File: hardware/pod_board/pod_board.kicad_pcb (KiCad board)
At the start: 4 copper layers, 80 x 55 mm, 0 parts

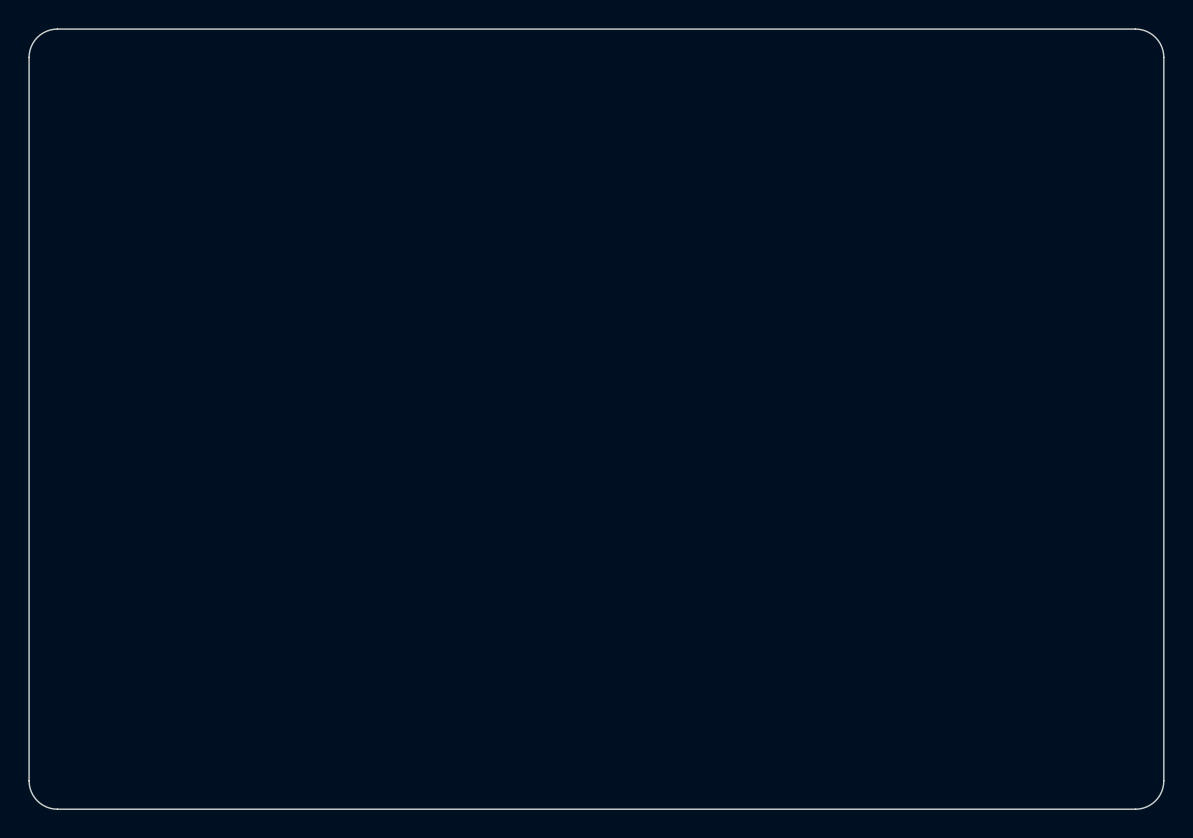
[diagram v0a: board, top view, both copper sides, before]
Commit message: PCBs routed, labelled and ready to order: Rev 1 fabrication files and buy list
Both boards placed, routed and finished by script (hardware/gen): layout.sh places
(placement.py, with silkscreen names for every terminal, port, header and button),
route.sh routes with Freerouting inside rule areas and net classes from the layout
guide and keeps a board only with 0 DRC errors, 0 unconnected and exact schematic
parity, routespec.sh checks what the DRC cannot (planes, crystal, converter loop,
IPC-2221 widths), finish.sh adds the bottom-silkscreen identification and writes
the fabrication files (gerbers, drill, BOM, positions) only when the DRC passes.

- Pod 70 x 53 mm, 4 layers: In1 solid GND, In2 +3V3, 530 teardrops; no DRC warnings.
- Power 95 x 66 mm, 2 layers, 2 oz: 10 A rail as a zone, converter re-placed (switch
  node 16 mm, feedback 7 mm, no vias; was 78 mm and 40 mm), 328 teardrops.
- Screw terminals turned to open outward; RESET/BOOT side-push on the pod's left
  edge; USB-C footprint with a 3D model (GCT USB4105).
- Pod J2 now the Adafruit 4754's JP1 row pin for pin (the old order shorted its
  3.3 V output to ground); IMU reset on a new J8; HC-05 header fed 5 V.
- Buy list per footprint and module connections in bill-of-materials.md section 10.
- LAYOUT_GUIDE rewritten as how the boards were routed and how to review them;
  decisions, progress log and BUILD_GUIDE updated; power box follows the wider board.
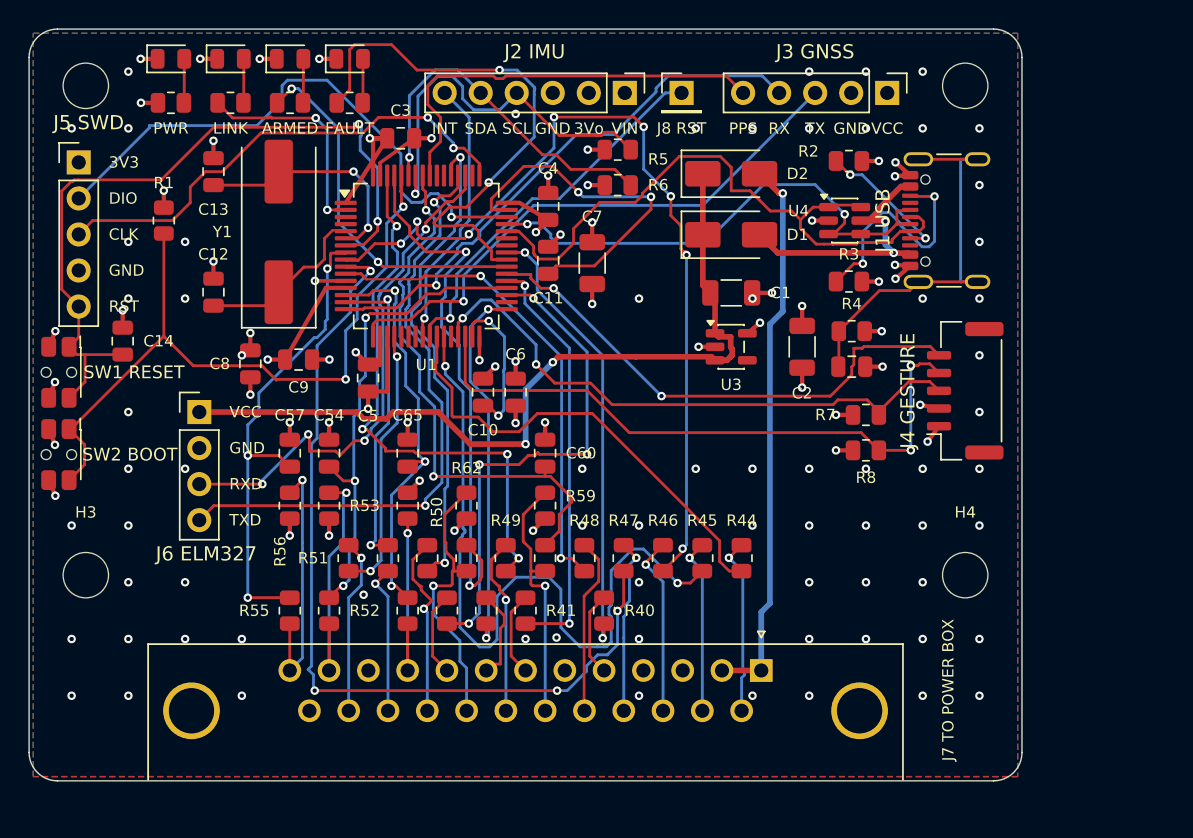
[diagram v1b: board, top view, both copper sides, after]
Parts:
- added C1: 10u, Capacitor_SMD:C_1206_3216Metric, F.Cu at (99.5, 68.6)
- added C10: 2.2u, Capacitor_SMD:C_0805_2012Metric, F.Cu at (82.0, 75.6)
- added C11: 2.2u, Capacitor_SMD:C_0805_2012Metric, F.Cu at (86.6, 66.3)
- added C12: 15p, Capacitor_SMD:C_0805_2012Metric, F.Cu at (63.0, 68.5)
- added C13: 15p, Capacitor_SMD:C_0805_2012Metric, F.Cu at (63.0, 60.0)
- added C14: 100n, Capacitor_SMD:C_0805_2012Metric, F.Cu at (56.6, 72.0)
- added C15: 4.7n, Capacitor_SMD:C_0805_2012Metric, F.Cu at (108.0, 73.8)
- added C2: 10u, Capacitor_SMD:C_1206_3216Metric, F.Cu at (104.5, 72.4)
- added C3: 100n, Capacitor_SMD:C_0805_2012Metric, F.Cu at (76.2, 57.7)
- added C4: 100n, Capacitor_SMD:C_0805_2012Metric, F.Cu at (86.6, 62.5)
- added C5: 100n, Capacitor_SMD:C_0805_2012Metric, F.Cu at (73.9, 74.6)
- added C54: 10n, Capacitor_SMD:C_0805_2012Metric, F.Cu at (71.2, 79.9)
- added C57: 10n, Capacitor_SMD:C_0805_2012Metric, F.Cu at (68.4, 79.9)
- added C6: 100n, Capacitor_SMD:C_0805_2012Metric, F.Cu at (84.3, 75.6)
- added C60: 10n, Capacitor_SMD:C_0805_2012Metric, F.Cu at (86.4, 79.9)
- added C65: 100n, Capacitor_SMD:C_0805_2012Metric, F.Cu at (76.7, 79.9)
- added C7: 4.7u, Capacitor_SMD:C_1206_3216Metric, F.Cu at (89.7, 66.5)
- added C8: 1u, Capacitor_SMD:C_0805_2012Metric, F.Cu at (65.6, 73.6)
- added C9: 100n, Capacitor_SMD:C_0805_2012Metric, F.Cu at (69.0, 73.3)
- added D1: SS14, Diode_SMD:D_SMA, F.Cu at (99.5, 64.5)
- added D2: SS14, Diode_SMD:D_SMA, F.Cu at (99.5, 60.2)
- added D3: green, LED_SMD:LED_0805_2012Metric, F.Cu at (60.0, 52.1)
- added D4: blue, LED_SMD:LED_0805_2012Metric, F.Cu at (64.2, 52.1)
- added D5: amber, LED_SMD:LED_0805_2012Metric, F.Cu at (68.4, 52.1)
- added D6: red, LED_SMD:LED_0805_2012Metric, F.Cu at (72.6, 52.1)
- added H1: M3, MountingHole:MountingHole_3.2mm_M3, F.Cu at (54.0, 54.0)
- added H2: M3, MountingHole:MountingHole_3.2mm_M3, F.Cu at (116.0, 54.0)
- added H3: M3, MountingHole:MountingHole_3.2mm_M3, F.Cu at (54.0, 88.5)
- added H4: M3, MountingHole:MountingHole_3.2mm_M3, F.Cu at (116.0, 88.5)
- added J1: USB-C, Connector_USB:USB_C_Receptacle_GCT_USB4105-xx-A_16P_TopMnt_Horizontal, F.Cu at (115.8, 63.5)
- added J2: IMU (BNO085 breakout), Connector_PinHeader_2.54mm:PinHeader_1x06_P2.54mm_Vertical, F.Cu at (92.0, 54.5)
- added J3: GNSS (NEO-M8N breakout), Connector_PinHeader_2.54mm:PinHeader_1x05_P2.54mm_Vertical, F.Cu at (110.5, 54.5)
- added J4: Gesture puck (JST-GH), Connector_JST:JST_GH_SM05B-GHS-TB_1x05-1MP_P1.25mm_Horizontal, F.Cu at (116.0, 75.5)
- added J5: SWD (ST-Link), Connector_PinHeader_2.54mm:PinHeader_1x05_P2.54mm_Vertical, F.Cu at (53.5, 59.4)
- added J6: ELM327 fallback (USART3), Connector_PinHeader_2.54mm:PinHeader_1x04_P2.54mm_Vertical, F.Cu at (62.0, 77.0)
- added J7: DB-25 to power box, Connector_Dsub:DSUB-25_Socket_Horizontal_P2.77x2.84mm_EdgePinOffset4.94mm_Housed_MountingHolesOffset4.94mm, F.Cu at (101.6, 95.2)
- added J8: IMU reset (optional wire), Connector_PinHeader_2.54mm:PinHeader_1x01_P2.54mm_Vertical, F.Cu at (96.0, 54.5)
- added R1: 10k, Resistor_SMD:R_0805_2012Metric, F.Cu at (59.5, 63.5)
- added R2: 5.1k, Resistor_SMD:R_0805_2012Metric, F.Cu at (107.8, 59.3)
- added R3: 5.1k, Resistor_SMD:R_0805_2012Metric, F.Cu at (107.8, 67.8)
- added R30: 1k, Resistor_SMD:R_0805_2012Metric, F.Cu at (60.0, 55.2)
- added R31: 1k, Resistor_SMD:R_0805_2012Metric, F.Cu at (64.2, 55.2)
- added R32: 1k, Resistor_SMD:R_0805_2012Metric, F.Cu at (68.4, 55.2)
- added R33: 1k, Resistor_SMD:R_0805_2012Metric, F.Cu at (72.6, 55.2)
- added R4: 1M, Resistor_SMD:R_0805_2012Metric, F.Cu at (108.0, 71.3)
- added R40: 1k, Resistor_SMD:R_0805_2012Metric, F.Cu at (90.5, 91.0)
- added R41: 1k, Resistor_SMD:R_0805_2012Metric, F.Cu at (85.0, 91.0)
- added R42: 1k, Resistor_SMD:R_0805_2012Metric, F.Cu at (82.2, 91.0)
- added R43: 1k, Resistor_SMD:R_0805_2012Metric, F.Cu at (79.5, 91.0)
- added R44: 1k, Resistor_SMD:R_0805_2012Metric, F.Cu at (100.2, 87.3)
- added R45: 1k, Resistor_SMD:R_0805_2012Metric, F.Cu at (97.5, 87.3)
- added R46: 1k, Resistor_SMD:R_0805_2012Metric, F.Cu at (94.7, 87.3)
- added R47: 1k, Resistor_SMD:R_0805_2012Metric, F.Cu at (91.9, 87.3)
- added R48: 1k, Resistor_SMD:R_0805_2012Metric, F.Cu at (89.2, 87.3)
- added R49: 330, Resistor_SMD:R_0805_2012Metric, F.Cu at (83.6, 87.3)
- added R5: 4.7k, Resistor_SMD:R_0805_2012Metric, F.Cu at (91.5, 58.5)
- added R50: 1k, Resistor_SMD:R_0805_2012Metric, F.Cu at (78.1, 87.3)
- added R51: 1k, Resistor_SMD:R_0805_2012Metric, F.Cu at (72.5, 87.3)
- added R52: 1k, Resistor_SMD:R_0805_2012Metric, F.Cu at (71.2, 91.0)
- added R53: 10k, Resistor_SMD:R_0805_2012Metric, F.Cu at (71.2, 83.6)
- added R55: 1k, Resistor_SMD:R_0805_2012Metric, F.Cu at (68.4, 91.0)
- added R56: 10k, Resistor_SMD:R_0805_2012Metric, F.Cu at (68.4, 83.6)
- added R58: 1k, Resistor_SMD:R_0805_2012Metric, F.Cu at (86.4, 87.3)
- added R59: 10k, Resistor_SMD:R_0805_2012Metric, F.Cu at (86.4, 83.6)
- added R6: 4.7k, Resistor_SMD:R_0805_2012Metric, F.Cu at (91.5, 61.0)
- added R61: 100, Resistor_SMD:R_0805_2012Metric, F.Cu at (80.8, 87.3)
- added R62: 10k, Resistor_SMD:R_0805_2012Metric, F.Cu at (80.8, 83.6)
- added R63: 100, Resistor_SMD:R_0805_2012Metric, F.Cu at (75.3, 87.3)
- added R64: 1k, Resistor_SMD:R_0805_2012Metric, F.Cu at (76.7, 91.0)
- added R66: 100k, Resistor_SMD:R_0805_2012Metric, F.Cu at (76.7, 83.6)
- added R7: 2.2k, Resistor_SMD:R_0805_2012Metric, F.Cu at (109.0, 77.2)
- added R8: 2.2k, Resistor_SMD:R_0805_2012Metric, F.Cu at (109.0, 79.7)
- added SW1: RESET, Button_Switch_SMD:SW_SPST_EVQP7C, F.Cu at (52.1, 74.2)
- added SW2: BOOT, Button_Switch_SMD:SW_SPST_EVQP7C, F.Cu at (52.1, 80.0)
- added U1: STM32F405RGT6, Package_QFP:LQFP-64_10x10mm_P0.5mm, F.Cu at (78.0, 66.0)
- added U3: AP2112K-3.3, Package_TO_SOT_SMD:SOT-23-5, F.Cu at (99.5, 72.4)
- added U4: USBLC6-2SC6, Package_TO_SOT_SMD:SOT-23-6, F.Cu at (107.5, 63.5)
- added Y1: 8MHz, Crystal:Crystal_SMD_HC49-SD, F.Cu at (67.6, 64.3)
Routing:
- net /RELAY_HAZARD: track 0.00 -> 61.9 mm, vias 0 -> 8
- net /RELAY_HORN: track 0.00 -> 61.9 mm, vias 0 -> 4
- net /VIN_POD: track 0.00 -> 58.1 mm, vias 0 -> 2
- net GND: track 0.00 -> 54.4 mm, vias 0 -> 109
- net /RELAY_RIGHT: track 0.00 -> 53.6 mm, vias 0 -> 2
- net /NRST: track 0.00 -> 53.0 mm, vias 0 -> 2
- net +3V3: track 0.00 -> 52.3 mm, vias 0 -> 22
- net /MCU: STM32F405RGT6/BOOT0: track 0.00 -> 51.4 mm, vias 0 -> 2
- net /GEST_SDA: track 0.00 -> 44.9 mm, vias 0 -> 2
- net /USB_DM: track 0.00 -> 44.9 mm
- net /OBD_RX: track 0.00 -> 43.5 mm, vias 0 -> 2
- net /GEST_SCL: track 0.00 -> 41.3 mm, vias 0 -> 2
- net /SWDIO: track 0.00 -> 40.8 mm, vias 0 -> 1
- net /GPS_RX: track 0.00 -> 39.9 mm, vias 0 -> 1
- net /CAN_TX: track 0.00 -> 39.7 mm, vias 0 -> 4
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- added copper zone on In2.Cu, net +3V3
- added copper zone on B.Cu, net GND
- added copper zone on F.Cu, net GND
- added copper zone on In1.Cu, net GND
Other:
- board size 80 x 55 mm -> 70 x 53 mm
- board text added: "3V3"
- board text added: "3Vo"
- board text added: "AR WINDSCREEN - POD BOARD"
- board text added: "ARMED"
- board text added: "CLK"
- board text added: "DIO"
- board text added: "FAULT"
- board text added: "GND"
- board text added: "Gesture cable (J4): right edge, below the USB"
- board text added: "I. K. MWENDA (FINAL YEAR PROJECT)"
- board text added: "INT"
- board text added: "J1 USB"
- board text added: "J2 IMU"
- board text added: "J3 GNSS"
- board text added: "J4 GESTURE"
- board text added: "J5 SWD"
- board text added: "J6 ELM327"
- board text added: "J7 TO POWER BOX"
- board text added: "J8 RST"
- board text added: "LINK"
- board text added: "PPS"
- board text added: "PWR"
- board text added: "REV 1 2026-10"
- board text added: "RST"
- board text added: "RX"
- board text added: "RXD"
- board text added: "SCL"
- board text added: "SDA"
- board text added: "SW1 RESET"
- board text added: "SW2 BOOT"
- board text added: "SWD header (J5) and the RESET/BOOT plungers (SW1, SW2): left edge"
- board text added: "TX"
- board text added: "TXD"
- board text added: "VCC"
- board text added: "VIN"
- board text added: "pod_board: 70 x 53 mm, 4 layers. 4 layers: signal / GND / +3V3 / signal. Ground plane unbroken under GNSS and IMU. Outline and holes from hardware/gen/outlines.py (shared with the enclosures)."
- board text removed: "SWD (J5) and ELM327 (J6) headers: left edge"
- board text removed: "pod_board: 80 x 55 mm, 4 layers. 4 layers: signal / GND / +3V3 / signal. Ground plane unbroken under GNSS and IMU. Outline and holes from hardware/gen/outlines.py (shared with the enclosures)."

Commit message: Review fixes: no via in SMD pads, 0.6 mm round terminal pins; 5 V converter simulated
An engineer's review of the Rev 1 boards: a via on a ground pad, and thin tracks
close to the screw terminals. Both measured true (9 vias touching ground pads on
the power board, 2 on the pod; 5 places within 0.3 mm of a terminal pin).

- route.py: no via touches any surface-mount pad (stitching and mending had let a
  via sit on its own net's pad); 0.6 mm round terminal and fuse-holder pins, given
  to Freerouting as grown pad copies (KiCad does not export a pad's own clearance);
  layout.py sets that clearance on the real pads for the DRC.
- routespec.sh checks both rules; both boards rerouted, teardrops re-added,
  finished: DRC 0 errors, 0 unconnected, parity exact; all checks pass.
- hardware/sim: the power board's TPS54360 converter simulated with TI's own
  transient model and the board's values, in KiCad's ngspice (no install):
  start-up, a 0.2-1.5 A load step (stability) and 9-30 V input, all within the
  stated limits. TI's model is downloaded on use, not committed.
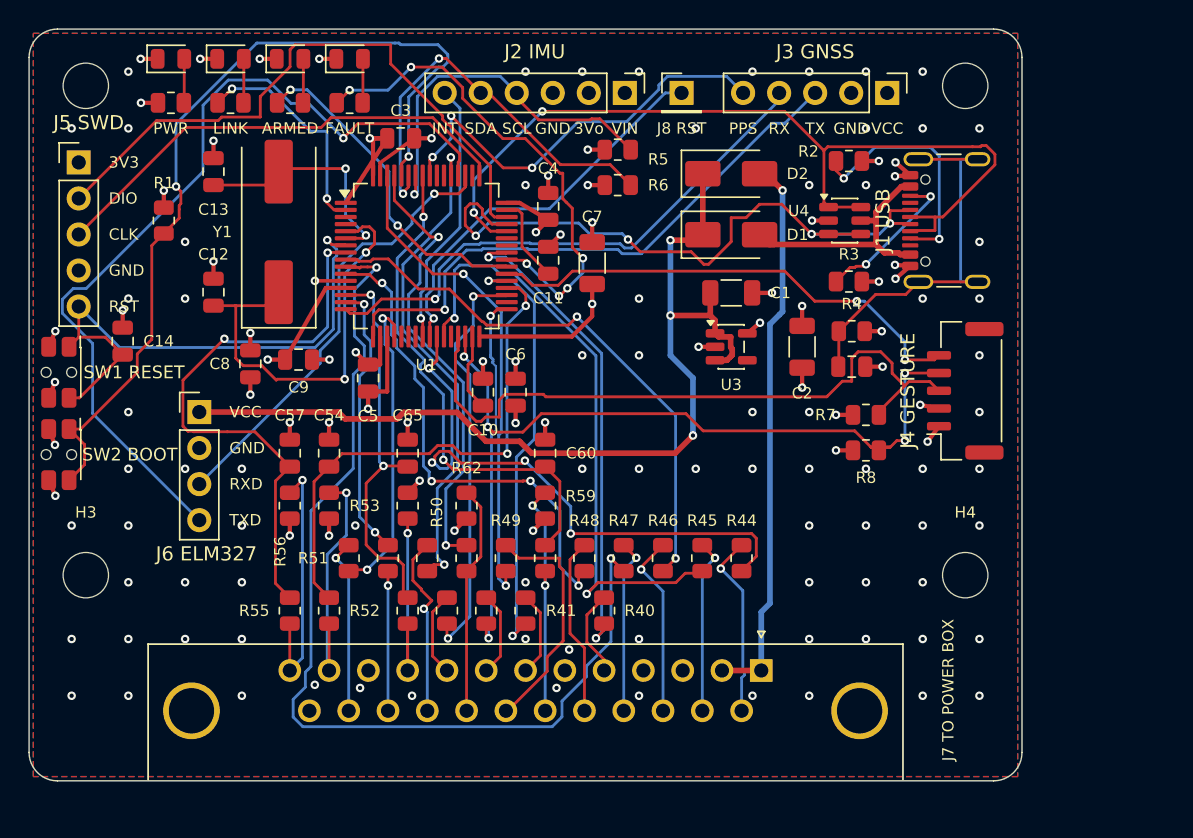
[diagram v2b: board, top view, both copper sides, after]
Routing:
- net /RELAY_HAZARD: track 61.9 -> 39.8 mm, vias 8 -> 2
- net /MCU: STM32F405RGT6/VCAP2: track 25.0 -> 6.18 mm, vias 2 -> 0
- net /MCU: STM32F405RGT6/OSC_IN: track 12.4 -> 30.6 mm, vias 0 -> 2
- net /USB_DM: track 44.9 -> 62.9 mm, vias 0 -> 2
- net /OBD_RX: track 43.5 -> 61.3 mm, vias 2 -> 1
- net /NRST: track 53.0 -> 39.6 mm, vias 2 -> 1
- net /USB_DP: track 37.2 -> 48.1 mm, vias 2 -> 4
- net /MCU: STM32F405RGT6/BOOT0: track 51.4 -> 61.8 mm
- net /RELAY_RIGHT: track 53.6 -> 43.8 mm
- net /VIN_POD: track 58.1 -> 67.8 mm, vias 2 -> 3
- net /RELAY_LEFT: track 33.0 -> 41.5 mm, vias 0 -> 4
- net /RELAY_HORN: track 61.9 -> 70.4 mm, vias 4 -> 2
- net +3V3: track 52.3 -> 60.0 mm, vias 22 -> 21
- net /USB-C to the laptop/USB_CC1: track 9.66 -> 17.3 mm
- net /GEST_SCL: track 41.3 -> 47.7 mm, vias 2 -> 0
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
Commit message: Enclosures, brake-light and pod-supply simulations, R63/C1/C2 values, report drafts
Enclosures (hardware/enclosures/): the E-stop housing (yellow ASA box for the 22 mm
mushroom, M16 gland, base to a dash panel), the windscreen pod (rear cover, front shell
whose carrier wall holds board and camera, black front plate with hood, cradle with a
+-8 deg pitch lock on a rail, glass plate template) and the gesture puck (APDS-9960
module under an open window, VHB base). Typical part dimensions are marked VERIFY.
Every STL is a manifold solid.

Simulations: run_brake.sh (PC817 input through the cable to PB5: thresholds with the
weakest and strongest optocoupler, reversed wiring, jump-start, load dump, timing) and
run_pod_supply.sh (cable +5 V and USB diode-OR into the AP2112K: worst cable, lowest
USB, cable pulled while running, USB inrush, back-feed). Both ALL PASS.

Adopted from them, value changes only (copper and teardrops untouched, fab files
regenerated, DRC 0/0, parity exact): power board R63 2.2k -> 4.7k (237 mW in a 24 V
jump-start, beyond the 0805's 125 mW; now 111 mW) and pod C1/C2 10u -> 1u/4.7u (USB
attach inrush 88 uC against USB 2.0's 50 uC; now 28 uC). Order from this commit: the
pcb-rev1.1 tag predates these two changes.

Report: docs/report/final/ drafts Part 16.1 sections 2-6 and 11 from the design as
built, with [RESULT]/[FIGURE]/[CHECK] slots where tests or decisions are pending.
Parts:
- C1: value 10u -> 1u
- C2: value 10u -> 4.7u
